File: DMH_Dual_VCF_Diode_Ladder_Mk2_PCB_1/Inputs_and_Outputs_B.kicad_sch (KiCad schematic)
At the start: 8 parts, among them J10 TS_Jack_6.35mm_Sw, J11 TS_Jack_6.35mm_Sw, J12 TS_Jack_6.35mm_Sw, J13 TS_Jack_6.35mm_Sw, J14 TS_Jack_6.35mm_Sw, J210 IDC_02x05, J8 TS_Jack_6.35mm_Sw, J9 TS_Jack_6.35mm_Sw

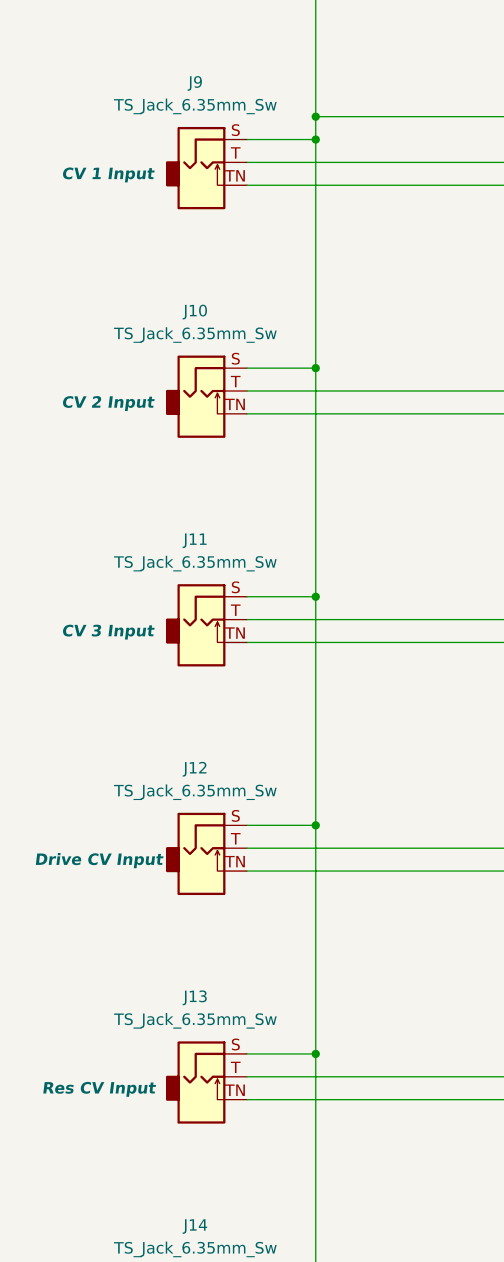
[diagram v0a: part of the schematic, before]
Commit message: Routed circuit B
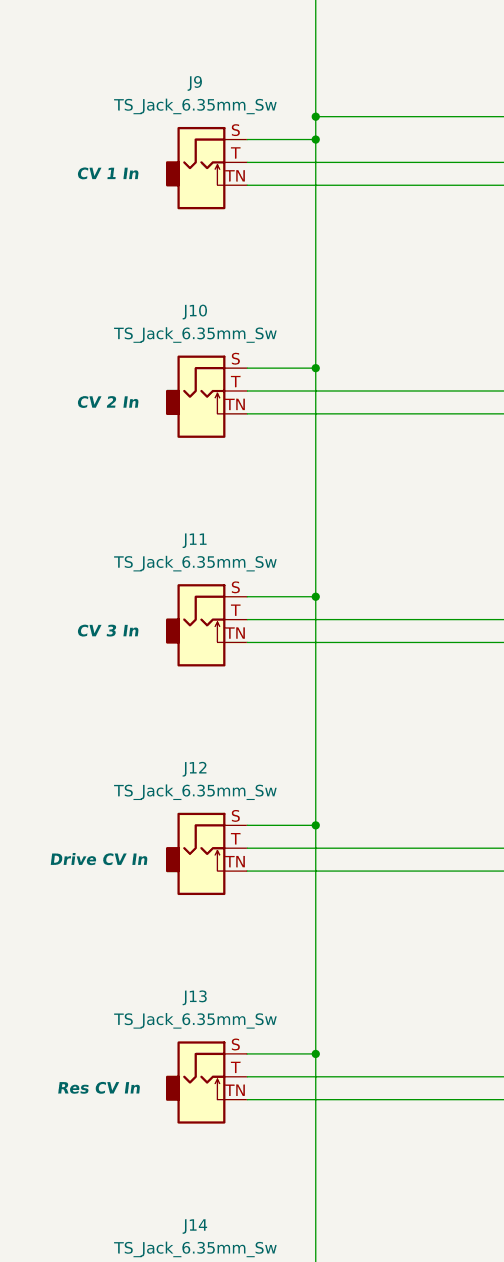
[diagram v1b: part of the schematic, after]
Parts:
- J10: Function CV 2 Input -> CV 2 In
- J11: Function CV 3 Input -> CV 3 In
- J12: Function Drive CV Input -> Drive CV In
- J13: Function Res CV Input -> Res CV In
- J9: Function CV 1 Input -> CV 1 In
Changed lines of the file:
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@@
 			)
 		)
-		(property "Function" "CV 2 Input"
+		(property "Function" "CV 2 In"
 			(at 40.386 90.17 0)
 			(effects
@@
 			)
 		)
-		(property "Function" "Drive CV Input"
+		(property "Function" "Drive CV In"
 			(at 39.37 140.97 0)
 			(effects
@@
 			)
 		)
-		(property "Function" "CV 1 Input"
+		(property "Function" "CV 1 In"
 			(at 40.386 64.77 0)
 			(effects
@@
 			)
 		)
-		(property "Function" "CV 3 Input"
+		(property "Function" "CV 3 In"
 			(at 40.386 115.57 0)
 			(effects
@@
 			)
 		)
-		(property "Function" "Res CV Input"
+		(property "Function" "Res CV In"
 			(at 39.37 166.37 0)
 			(effects
